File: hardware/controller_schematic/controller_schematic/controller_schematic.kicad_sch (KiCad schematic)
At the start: 7 parts, among them U1 NRF24L01

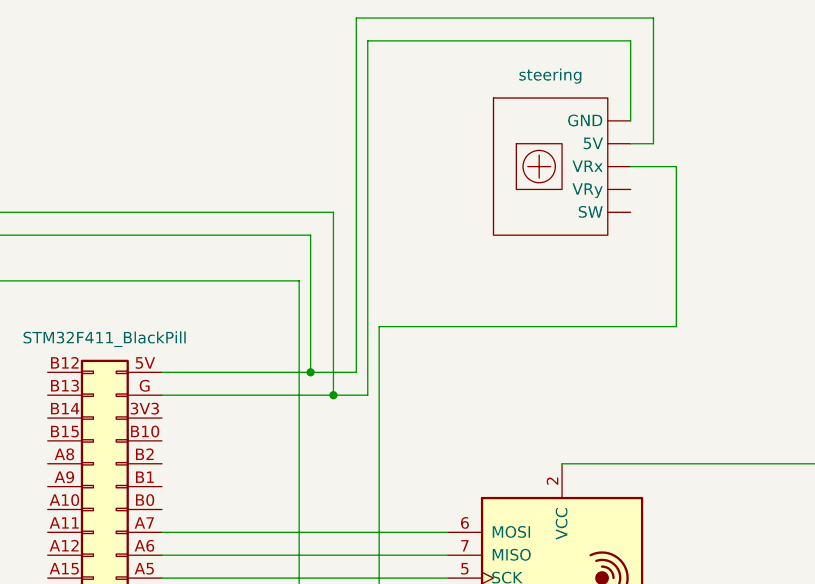
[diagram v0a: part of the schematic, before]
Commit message: update: update controller schematic for 2 axis to 3.3v instead of 5v
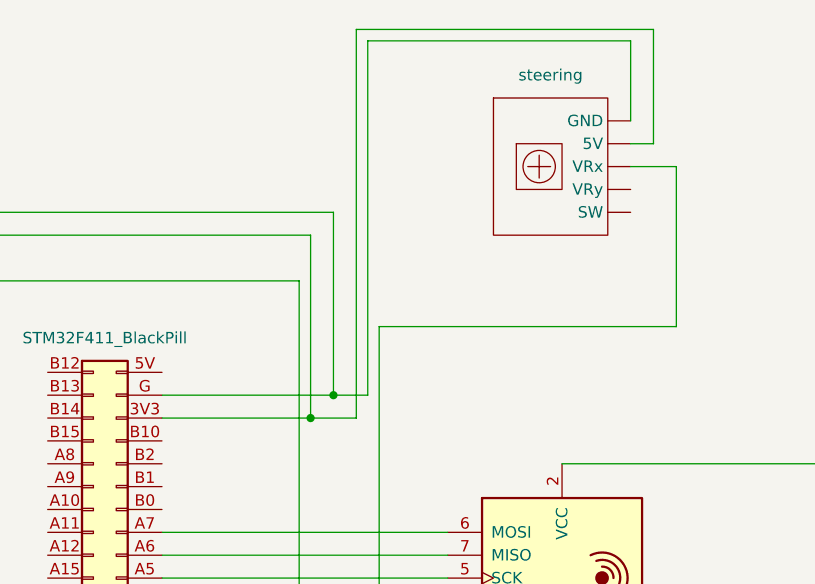
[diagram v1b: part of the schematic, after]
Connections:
- net at 5v_stepup. (VIN-): now also dsfds.2 (-); no longer STM32F411_BlackPill1.5V (Pin_40)
- net at STM32F411_BlackPill1.3V3 (Pin_38): now also Throttle. (SW), steering. (SW)
- new net: 5v_stepup. (VIN-), STM32F411_BlackPill1.5V (Pin_40)
- new net: STM32F411_BlackPill1.G (Pin_39), Throttle. (SW), steering. (SW)
- now unconnected: STM32F411_BlackPill1.5V (Pin_40), Throttle. (SW), Throttle. (SW), steering. (SW), steering. (SW)
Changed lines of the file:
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@@
 	(paper "A4")
+	(junction
+		(at 140.97 74.93)
+		(diameter 0)
+		(color 0 0 0 0)
+	)
 	(junction
 		(at 143.51 72.39)
@@
 	)
 	(junction
-		(at 140.97 69.85)
-		(diameter 0)
-		(color 0 0 0 0)
-	)
-	(junction
 		(at 168.91 120.65)
 		(diameter 0)
@@
 	(wire
 		(pts
-			(xy 179.07 30.48) (xy 146.05 30.48)
-		)
-		(stroke
-			(width 0)
-			(type default)
-		)
-	)
-	(wire
-		(pts
-			(xy 140.97 69.85) (xy 124.46 69.85)
-		)
-		(stroke
-			(width 0)
-			(type default)
-		)
-	)
-	(wire
-		(pts
 			(xy 82.55 52.07) (xy 143.51 52.07)
 		)
@@
 	(wire
 		(pts
-			(xy 140.97 54.61) (xy 140.97 69.85)
-		)
-		(stroke
-			(width 0)
-			(type default)
-		)
-	)
-	(wire
-		(pts
-			(xy 179.07 44.45) (xy 179.07 30.48)
+			(xy 140.97 54.61) (xy 140.97 74.93)
+		)
+		(stroke
+			(width 0)
+			(type default)
+		)
+	)
+	(wire
+		(pts
+			(xy 146.05 74.93) (xy 140.97 74.93)
 		)
 		(stroke
@@
 	(wire
 		(pts
+			(xy 146.05 31.75) (xy 146.05 74.93)
+		)
+		(stroke
+			(width 0)
+			(type default)
+		)
+	)
+	(wire
+		(pts
 			(xy 147.32 72.39) (xy 143.51 72.39)
 		)
@@
 	(wire
 		(pts
+			(xy 179.07 31.75) (xy 146.05 31.75)
+		)
+		(stroke
+			(width 0)
+			(type default)
+		)
+	)
+	(wire
+		(pts
 			(xy 201.93 109.22) (xy 201.93 124.46)
 		)
@@
 	(wire
 		(pts
+			(xy 179.07 44.45) (xy 179.07 31.75)
+		)
+		(stroke
+			(width 0)
+			(type default)
+		)
+	)
+	(wire
+		(pts
 			(xy 124.46 95.25) (xy 156.21 95.25)
 		)
@@
 	(wire
 		(pts
+			(xy 124.46 74.93) (xy 140.97 74.93)
+		)
+		(stroke
+			(width 0)
+			(type default)
+		)
+	)
+	(wire
+		(pts
 			(xy 168.91 80.01) (xy 201.93 80.01)
 		)
@@
 	(wire
 		(pts
+			(xy 176.53 44.45) (xy 179.07 44.45)
+		)
+		(stroke
+			(width 0)
+			(type default)
+		)
+	)
+	(wire
+		(pts
 			(xy 109.22 115.57) (xy 111.76 115.57)
 		)
@@
 	(wire
 		(pts
-			(xy 176.53 44.45) (xy 179.07 44.45)
-		)
-		(stroke
-			(width 0)
-			(type default)
-		)
-	)
-	(wire
-		(pts
-			(xy 146.05 30.48) (xy 146.05 69.85)
-		)
-		(stroke
-			(width 0)
-			(type default)
-		)
-	)
-	(wire
-		(pts
 			(xy 147.32 33.02) (xy 147.32 72.39)
 		)
@@
 		)
 		(stroke
-			(width 0)
-			(type default)
-		)
-	)
-	(wire
-		(pts
-			(xy 146.05 69.85) (xy 140.97 69.85)
-		)
-		(stroke
